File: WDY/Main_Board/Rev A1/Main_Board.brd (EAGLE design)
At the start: 130 x 70 mm, 194 parts, among them J1 22-05-7028-02, J10 22-05-7038-03, J11 22-05-7028-02, J12 22-05-7028-02, J13 22-05-7028-02, J14 22-05-7028-02, J15 22-05-7058-05, J16 22-27-2061-06, J2 22-05-7028-02, J3 22-05-7048-04, J4 22-05-7048-04, J5 1241050-5, J6 90814-0208, J7 90814-0206, J8 90814-0208, J9 22-05-7038-03, K1 G6K-2G-Y, K2 G6K-2G-Y, K3 G6K-2G-Y, K4 G6K-2G-Y, P1 RB1-125BAG1A, SW1 B3FS-1015, SW2 B3FS-1015, T1 MMBT2222AL, U1 LPC1768FBD100, U11 SN74LVC3G17DCTR, U2 SN74LVC3G17DCTR, U3 SN74LVC3G17DCTR, U4 TPL0401A, U5 AT24C512C-SSHM-B, U6 SN74LVC2G17DBVR, U7 SN74LVC2G17DBVR, U8 LT1767EMS8E-5PBF, U9 TC1264-3.3, X1 FC-135, X2 MSTBA2

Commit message: Fix : Test pad instead of solder jumper for WP (@2.E1) // Use BC-2-P in exmachina.lbr as a test
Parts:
- removed SJ3: SOLDERJUMPERNC2, SparkFun-Passives:SJ_2S-NOTRACE
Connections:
- net GND: now also JP1.2; no longer SJ3.1
- net N$22: now also JP1.1; no longer SJ3.2
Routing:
- net N$22: track 9.54 -> 6.02 mm
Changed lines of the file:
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@@
 <element name="U$9" library="frames" package="A4L-LOC" value="" x="-59" y="-24"/>
 <element name="R66" library="rcl" package="R0603" value="4k7" x="29" y="34.5" rot="R90"/>
-<element name="SJ3" library="SparkFun-Passives" package="SJ_2S-NOTRACE" value="SOLDERJUMPERNC2" x="23.2" y="28.6"/>
 <element name="U$10" library="crystal" package="ASE" value="ASE-12" x="74.5" y="25.5" rot="R90">
 <attribute name="OC_NEWARK" value="unknown" x="74.5" y="25.5" size="1.778" layer="27" rot="R90" display="off"/>
@@
 <wire x1="114.35" y1="58" x2="114" y2="58" width="0.4064" layer="1"/>
 <contactref element="U$3" pad="1"/>
-<contactref element="SJ3" pad="1"/>
 <contactref element="U$10" pad="2"/>
 <contactref element="U$10" pad="1"/>
@@
 <contactref element="J16" pad="1"/>
 <contactref element="TP3" pad="TP"/>
+<contactref element="JP1" pad="2"/>
+<wire x1="9.65" y1="33.8" x2="1.75" y2="42" width="0" layer="19" extent="1-1"/>
 </signal>
 <signal name="+3V3" class="2">
@@
 <contactref element="R66" pad="1"/>
 <contactref element="U5" pad="7"/>
-<contactref element="SJ3" pad="2"/>
 <wire x1="26.3622" y1="33.635" x2="26.3772" y2="33.65" width="0.1778" layer="1"/>
 <wire x1="26.3772" y1="33.65" x2="29" y2="33.65" width="0.1778" layer="1"/>
 <wire x1="26.3622" y1="33.635" x2="25.135" y2="33.635" width="0.1778" layer="1"/>
 <wire x1="25.135" y1="33.635" x2="23.6127" y2="32.1127" width="0.1778" layer="1"/>
-<wire x1="23.6127" y1="32.1127" x2="23.6127" y2="28.6" width="0.1778" layer="1"/>
+<contactref element="JP1" pad="1"/>
+<wire x1="1.75" y1="40" x2="23.6127" y2="32.1127" width="0" layer="19" extent="1-1"/>
 </signal>
 <signal name="N$65">

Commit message: Fix : Ethernet clock (@1.C8): TRI pin to VDD or NC to enable oscillator
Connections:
- net +3V3: now also U$3.1
- net GND: no longer U$3.1
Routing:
- net VBAT+: track 35.9 -> 4.83 mm, vias 3 -> 1
- net N$22: track 6.02 -> 34.0 mm, vias 0 -> 2
- net +3V3: track 153.4 -> 154.4 mm
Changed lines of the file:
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@@
 <layers>
 <layer number="1" name="Top" color="4" fill="1" visible="yes" active="yes"/>
-<layer number="2" name="Route2" color="6" fill="1" visible="yes" active="yes"/>
+<layer number="2" name="Route2" color="6" fill="1" visible="no" active="yes"/>
 <layer number="3" name="Route3" color="20" fill="1" visible="no" active="yes"/>
 <layer number="14" name="Route14" color="1" fill="6" visible="no" active="no"/>
@@
 <wire x1="115.35" y1="59" x2="114.35" y2="58" width="0.4064" layer="1"/>
 <wire x1="114.35" y1="58" x2="114" y2="58" width="0.4064" layer="1"/>
-<contactref element="U$3" pad="1"/>
 <contactref element="U$10" pad="2"/>
 <contactref element="U$10" pad="1"/>
@@
 <contactref element="TP3" pad="TP"/>
 <contactref element="JP1" pad="2"/>
-<wire x1="9.65" y1="33.8" x2="1.75" y2="42" width="0" layer="19" extent="1-1"/>
 </signal>
 <signal name="+3V3" class="2">
@@
 <via x="32.9" y="28.8" extent="1-16" drill="0.5"/>
 <wire x1="31.4" y1="34.25" x2="31.4" y2="35.9" width="0.4064" layer="1"/>
-<wire x1="29" y1="35.35" x2="29" y2="36.7" width="0.4064" layer="1"/>
+<wire x1="29" y1="35.35" x2="29" y2="36.4" width="0.4064" layer="1"/>
 <wire x1="26.3622" y1="34.905" x2="26.3622" y2="36.3378" width="0.4064" layer="1"/>
 <wire x1="26.3622" y1="36.3378" x2="26.1" y2="36.6" width="0.4064" layer="1"/>
@@
 <wire x1="25.5" y1="36.6" x2="26.1" y2="36.6" width="0.4064" layer="16"/>
 <via x="26.1" y="36.6" extent="1-16" drill="0.5"/>
-<via x="29" y="36.7" extent="1-16" drill="0.5"/>
+<via x="29" y="36.4" extent="1-16" drill="0.5"/>
 <via x="31.4" y="35.9" extent="1-16" drill="0.5"/>
 <wire x1="31.4" y1="29.25" x2="31.85" y2="28.8" width="0.4064" layer="1"/>
@@
 <wire x1="66.5" y1="24.36" x2="66.5" y2="23.3" width="0.4064" layer="16"/>
 <wire x1="66.5" y1="23.3" x2="66.2" y2="23" width="0.4064" layer="16"/>
-<wire x1="29" y1="32.58" x2="29" y2="36.7" width="0.4064" layer="16"/>
+<wire x1="29" y1="32.58" x2="29" y2="36.4" width="0.4064" layer="16"/>
 <wire x1="35.5" y1="33.8" x2="34.1" y2="33.8" width="0.4064" layer="1"/>
 <wire x1="34.1" y1="33.8" x2="33.5" y2="34.4" width="0.4064" layer="1"/>
+<contactref element="U$3" pad="1"/>
+<wire x1="30.35" y1="38.175" x2="30.35" y2="39.825" width="0.4064" layer="1"/>
 </signal>
 <signal name="N$4">
@@
 <wire x1="26.3772" y1="33.65" x2="29" y2="33.65" width="0.1778" layer="1"/>
 <wire x1="26.3622" y1="33.635" x2="25.135" y2="33.635" width="0.1778" layer="1"/>
-<wire x1="25.135" y1="33.635" x2="23.6127" y2="32.1127" width="0.1778" layer="1"/>
 <contactref element="JP1" pad="1"/>
-<wire x1="1.75" y1="40" x2="23.6127" y2="32.1127" width="0" layer="19" extent="1-1"/>
+<wire x1="1.75" y1="40" x2="12.5" y2="40" width="0.1778" layer="1"/>
+<via x="12.5" y="40" extent="1-16" drill="0.35"/>
+<wire x1="12.5" y1="40" x2="12.5" y2="36" width="0.1778" layer="16"/>
+<wire x1="12.5" y1="36" x2="17" y2="31.5" width="0.1778" layer="16"/>
+<wire x1="17" y1="31.5" x2="23" y2="31.5" width="0.1778" layer="16"/>
+<wire x1="25.135" y1="33.635" x2="24" y2="32.5" width="0.1778" layer="1"/>
+<via x="24" y="32.5" extent="1-16" drill="0.35"/>
+<wire x1="24" y1="32.5" x2="23" y2="31.5" width="0.1778" layer="16"/>
 </signal>
 <signal name="N$65">
@@
 <vertex x="18" y="42"/>
 </polygon>
-<wire x1="4.5" y1="61.374" x2="4.374" y2="54.374" width="0.4064" layer="16"/>
-<wire x1="4.374" y1="54.374" x2="3" y2="53" width="0.4064" layer="16"/>
-<wire x1="3" y1="53" x2="3" y2="41" width="0.4064" layer="16"/>
-<wire x1="3" y1="41" x2="3" y2="40" width="0.4064" layer="16"/>
-<wire x1="3" y1="40" x2="4.501" y2="38.499" width="0.4064" layer="16"/>
-<wire x1="4.501" y1="38.499" x2="4.5" y2="45.499" width="0.4064" layer="16"/>
-<via x="3" y="40" extent="1-16" drill="0.5"/>
-<via x="3" y="41" extent="1-16" drill="0.5"/>
 <wire x1="70.5" y1="28.88" x2="70.5" y2="32.5" width="0.4064" layer="1"/>
 <wire x1="70.5" y1="32.5" x2="71" y2="33" width="0.4064" layer="1"/>
 <wire x1="71" y1="33" x2="71.5" y2="33" width="0.4064" layer="1"/>
 <via x="71.5" y="33" extent="1-16" drill="0.5"/>
+<wire x1="4.5" y1="45.499" x2="4.5" y2="61.374" width="0" layer="19" extent="16-16"/>
+<wire x1="70.5" y1="32.5" x2="4.5" y2="45.499" width="0" layer="19" extent="1-16"/>
 </signal>
 <signal name="N$7">

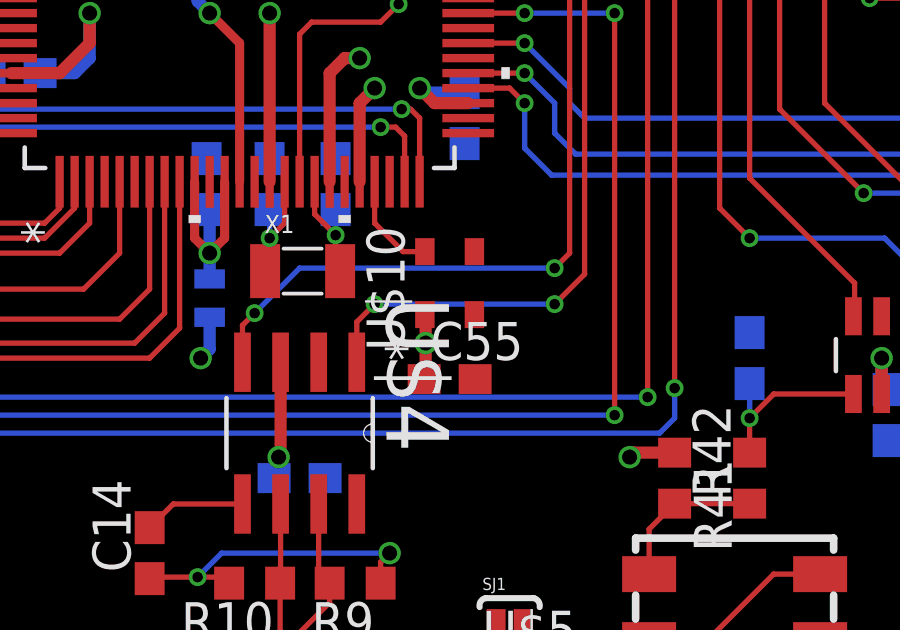
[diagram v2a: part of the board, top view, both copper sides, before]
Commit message: Fix : MCU clock (@2.C1): TRI pin to VDD or NC to enable oscillator
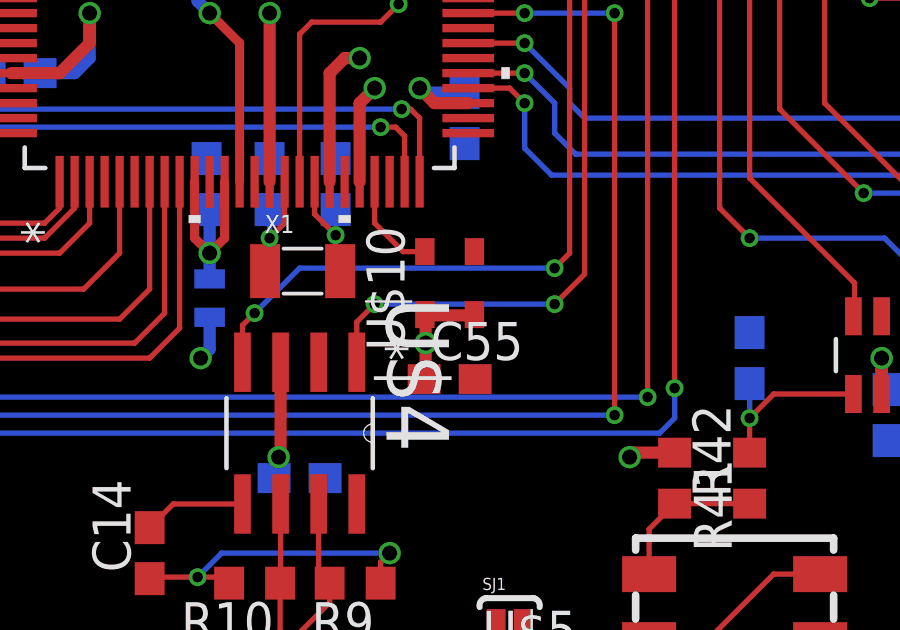
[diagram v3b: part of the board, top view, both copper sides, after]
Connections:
- net +3V3: now also U$10.1
- net GND: no longer U$10.1
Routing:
- net +3V3: track 154.4 -> 156.1 mm
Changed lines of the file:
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@@
 <layers>
 <layer number="1" name="Top" color="4" fill="1" visible="yes" active="yes"/>
-<layer number="2" name="Route2" color="6" fill="1" visible="no" active="yes"/>
+<layer number="2" name="Route2" color="6" fill="1" visible="yes" active="yes"/>
 <layer number="3" name="Route3" color="20" fill="1" visible="no" active="yes"/>
 <layer number="14" name="Route14" color="1" fill="6" visible="no" active="no"/>
 <layer number="15" name="Route15" color="4" fill="6" visible="no" active="no"/>
-<layer number="16" name="Bottom" color="1" fill="1" visible="yes" active="yes"/>
+<layer number="16" name="Bottom" color="1" fill="1" visible="no" active="yes"/>
 <layer number="17" name="Pads" color="2" fill="1" visible="yes" active="yes"/>
 <layer number="18" name="Vias" color="2" fill="1" visible="yes" active="yes"/>
@@
 <layer number="20" name="Dimension" color="15" fill="1" visible="yes" active="yes"/>
 <layer number="21" name="tPlace" color="7" fill="1" visible="yes" active="yes"/>
-<layer number="22" name="bPlace" color="7" fill="1" visible="yes" active="yes"/>
+<layer number="22" name="bPlace" color="7" fill="1" visible="no" active="yes"/>
 <layer number="23" name="tOrigins" color="15" fill="1" visible="yes" active="yes"/>
-<layer number="24" name="bOrigins" color="15" fill="1" visible="yes" active="yes"/>
+<layer number="24" name="bOrigins" color="15" fill="1" visible="no" active="yes"/>
 <layer number="25" name="tNames" color="7" fill="1" visible="yes" active="yes"/>
-<layer number="26" name="bNames" color="7" fill="1" visible="yes" active="yes"/>
+<layer number="26" name="bNames" color="7" fill="1" visible="no" active="yes"/>
 <layer number="27" name="tValues" color="7" fill="1" visible="yes" active="yes"/>
-<layer number="28" name="bValues" color="7" fill="1" visible="yes" active="yes"/>
+<layer number="28" name="bValues" color="7" fill="1" visible="no" active="yes"/>
 <layer number="29" name="tStop" color="7" fill="3" visible="no" active="yes"/>
 <layer number="30" name="bStop" color="7" fill="6" visible="no" active="yes"/>
@@
 <layer number="50" name="dxf" color="7" fill="1" visible="yes" active="yes"/>
 <layer number="51" name="tDocu" color="7" fill="1" visible="yes" active="yes"/>
-<layer number="52" name="bDocu" color="7" fill="1" visible="yes" active="yes"/>
+<layer number="52" name="bDocu" color="7" fill="1" visible="no" active="yes"/>
 <layer number="53" name="tGND_GNDA" color="7" fill="1" visible="yes" active="yes"/>
 <layer number="54" name="bGND_GNDA" color="7" fill="1" visible="yes" active="yes"/>
@@
 <wire x1="114.35" y1="58" x2="114" y2="58" width="0.4064" layer="1"/>
 <contactref element="U$10" pad="2"/>
-<contactref element="U$10" pad="1"/>
 <contactref element="C55" pad="2"/>
 <contactref element="R12" pad="1"/>
@@
 <contactref element="U$3" pad="1"/>
 <wire x1="30.35" y1="38.175" x2="30.35" y2="39.825" width="0.4064" layer="1"/>
+<contactref element="U$10" pad="1"/>
+<wire x1="73.7" y1="24.425" x2="75.3" y2="24.425" width="0.4064" layer="1"/>
+<wire x1="75.3" y1="24.425" x2="75.325" y2="24.45" width="0.4064" layer="1"/>
 </signal>
 <signal name="N$4">

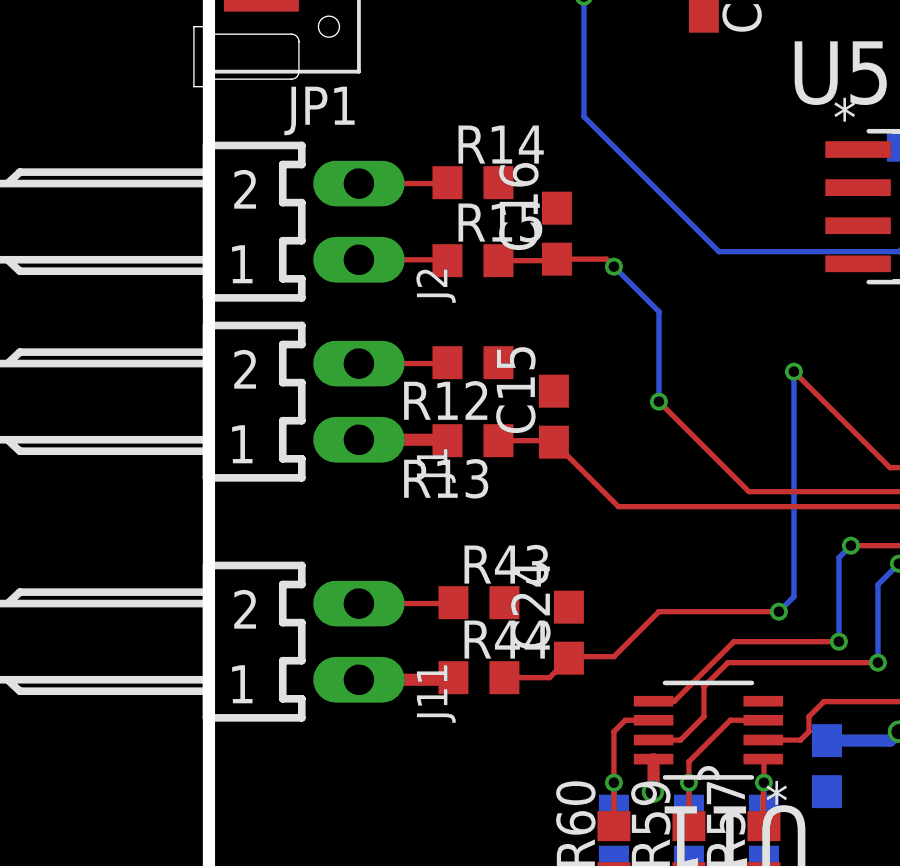
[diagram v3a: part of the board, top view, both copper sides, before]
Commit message: Fix : Thermistor switch sense net between R12/14 and J1-2/2-2
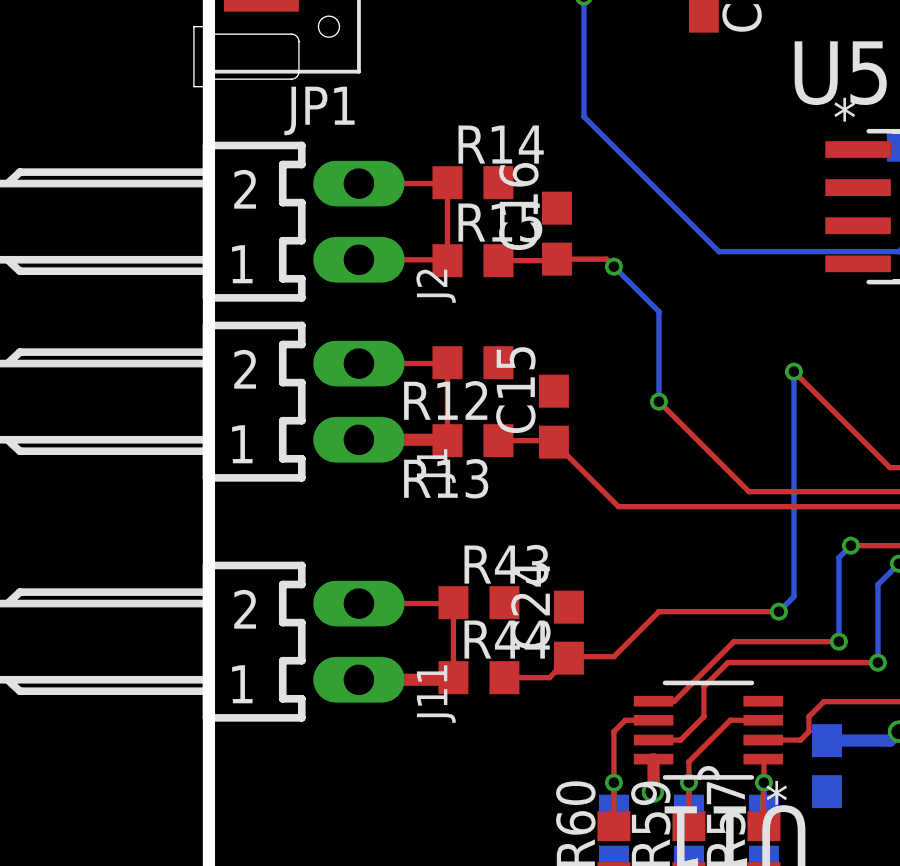
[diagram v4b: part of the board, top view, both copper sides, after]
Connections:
- net AVDD: no longer R13.2, R15.1, R44.1
- net N$65: now also R13.2
- net N$66: now also R15.1
- net N$67: now also R44.1
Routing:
- net N$65: track 2.96 -> 5.56 mm
- net N$66: track 2.96 -> 5.56 mm
- net N$67: track 3.18 -> 5.68 mm
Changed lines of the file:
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@@
 <layers>
 <layer number="1" name="Top" color="4" fill="1" visible="yes" active="yes"/>
-<layer number="2" name="Route2" color="6" fill="1" visible="yes" active="yes"/>
+<layer number="2" name="Route2" color="6" fill="1" visible="no" active="yes"/>
 <layer number="3" name="Route3" color="20" fill="1" visible="no" active="yes"/>
 <layer number="14" name="Route14" color="1" fill="6" visible="no" active="no"/>
 <layer number="15" name="Route15" color="4" fill="6" visible="no" active="no"/>
-<layer number="16" name="Bottom" color="1" fill="1" visible="no" active="yes"/>
+<layer number="16" name="Bottom" color="1" fill="1" visible="yes" active="yes"/>
 <layer number="17" name="Pads" color="2" fill="1" visible="yes" active="yes"/>
 <layer number="18" name="Vias" color="2" fill="1" visible="yes" active="yes"/>
@@
 <layer number="20" name="Dimension" color="15" fill="1" visible="yes" active="yes"/>
 <layer number="21" name="tPlace" color="7" fill="1" visible="yes" active="yes"/>
-<layer number="22" name="bPlace" color="7" fill="1" visible="no" active="yes"/>
+<layer number="22" name="bPlace" color="7" fill="1" visible="yes" active="yes"/>
 <layer number="23" name="tOrigins" color="15" fill="1" visible="yes" active="yes"/>
-<layer number="24" name="bOrigins" color="15" fill="1" visible="no" active="yes"/>
+<layer number="24" name="bOrigins" color="15" fill="1" visible="yes" active="yes"/>
 <layer number="25" name="tNames" color="7" fill="1" visible="yes" active="yes"/>
-<layer number="26" name="bNames" color="7" fill="1" visible="no" active="yes"/>
+<layer number="26" name="bNames" color="7" fill="1" visible="yes" active="yes"/>
 <layer number="27" name="tValues" color="7" fill="1" visible="yes" active="yes"/>
-<layer number="28" name="bValues" color="7" fill="1" visible="no" active="yes"/>
+<layer number="28" name="bValues" color="7" fill="1" visible="yes" active="yes"/>
 <layer number="29" name="tStop" color="7" fill="3" visible="no" active="yes"/>
 <layer number="30" name="bStop" color="7" fill="6" visible="no" active="yes"/>
@@
 <layer number="50" name="dxf" color="7" fill="1" visible="yes" active="yes"/>
 <layer number="51" name="tDocu" color="7" fill="1" visible="yes" active="yes"/>
-<layer number="52" name="bDocu" color="7" fill="1" visible="no" active="yes"/>
+<layer number="52" name="bDocu" color="7" fill="1" visible="yes" active="yes"/>
 <layer number="53" name="tGND_GNDA" color="7" fill="1" visible="yes" active="yes"/>
 <layer number="54" name="bGND_GNDA" color="7" fill="1" visible="yes" active="yes"/>
@@
 <contactref element="U1" pad="10"/>
 <contactref element="U1" pad="12"/>
-<contactref element="R44" pad="1"/>
 <contactref element="J11" pad="1"/>
-<contactref element="R15" pad="1"/>
 <contactref element="J2" pad="1"/>
-<contactref element="R13" pad="2"/>
 <contactref element="J1" pad="1"/>
 <wire x1="5" y1="17.23" x2="8.15" y2="17.23" width="0.4064" layer="1"/>
-<wire x1="8.15" y1="17.23" x2="8.15" y2="17.3" width="0.4064" layer="1"/>
 <wire x1="5" y1="31.23" x2="7.92" y2="31.23" width="0.1778" layer="1"/>
-<wire x1="7.92" y1="31.23" x2="7.95" y2="31.2" width="0.1778" layer="1"/>
 <wire x1="5" y1="25.23" x2="7.92" y2="25.23" width="0.4064" layer="1"/>
-<wire x1="7.92" y1="25.23" x2="7.95" y2="25.2" width="0.4064" layer="1"/>
 <via x="66.5" y="26.5" extent="1-16" drill="0.5"/>
 <wire x1="66.4" y1="27.95" x2="66.5" y2="28.05" width="0.4064" layer="16"/>
@@
 <wire x1="5" y1="27.77" x2="7.92" y2="27.77" width="0.1778" layer="1"/>
 <wire x1="7.92" y1="27.77" x2="7.95" y2="27.8" width="0.1778" layer="1"/>
+<contactref element="R13" pad="2"/>
+<wire x1="7.95" y1="25.2" x2="7.95" y2="27.8" width="0.1778" layer="1"/>
 </signal>
 <signal name="N$66">
@@
 <wire x1="5" y1="33.77" x2="7.92" y2="33.77" width="0.1778" layer="1"/>
 <wire x1="7.92" y1="33.77" x2="7.95" y2="33.8" width="0.1778" layer="1"/>
+<contactref element="R15" pad="1"/>
+<wire x1="7.95" y1="31.2" x2="7.95" y2="33.8" width="0.1778" layer="1"/>
 </signal>
 <signal name="N$67">
@@
 <wire x1="5" y1="19.77" x2="8.15" y2="19.77" width="0.1778" layer="1"/>
 <wire x1="8.15" y1="19.77" x2="8.15" y2="19.8" width="0.1778" layer="1"/>
+<contactref element="R44" pad="1"/>
+<wire x1="8.15" y1="17.3" x2="8.15" y2="19.8" width="0.1778" layer="1"/>
 </signal>
 <signal name="RESET">
